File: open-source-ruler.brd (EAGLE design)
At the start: 86 x 54 mm, 65 parts, among them IC1 LT1007CS8, IC2 FT232RLSSOP, IC3 MDC3105DMT1, IC4 XMEGA16A4A, IC5 LFXP20E_XXF256, IC7 ADSP_BF531, Q4 ASF1, U1 V_REG_317DPACK, U2 ATMEGA168, U3 ATMEGA168MLF, U4 7432SE, X1 MINI-USB-UX60A-MB-5ST

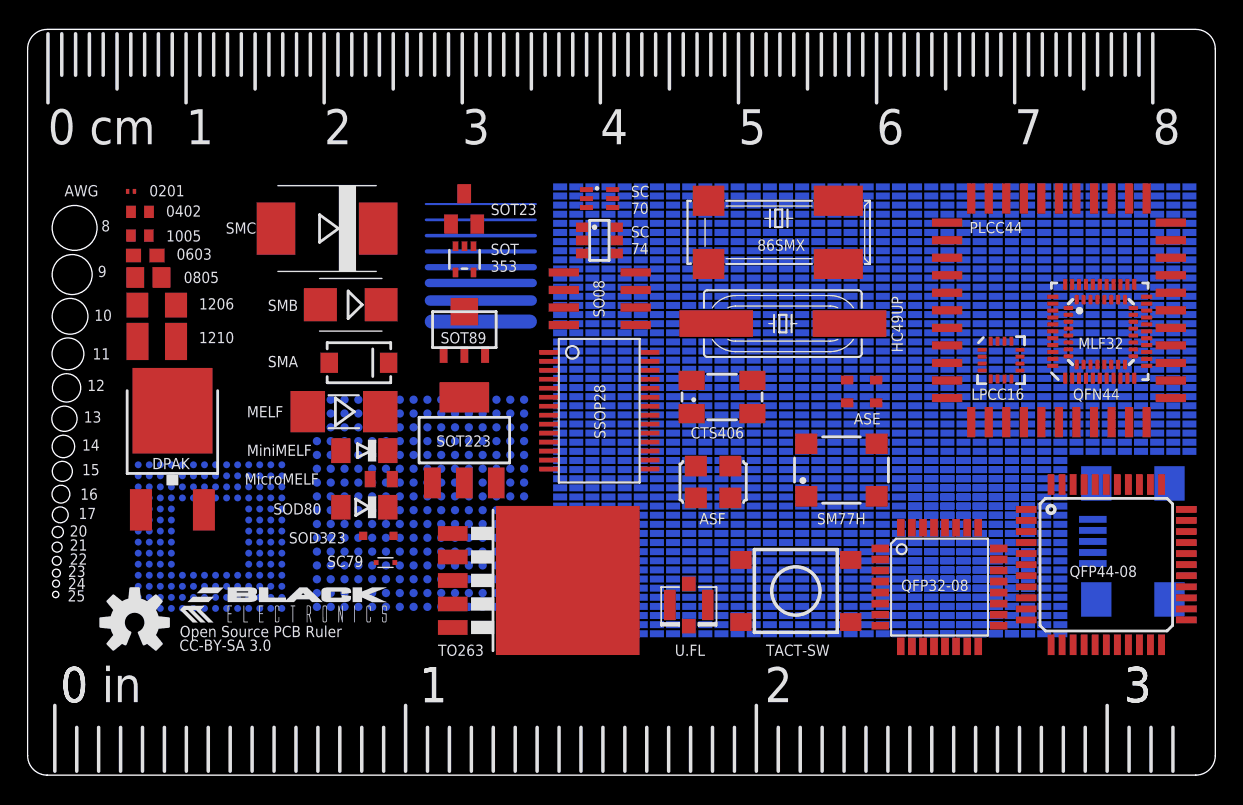
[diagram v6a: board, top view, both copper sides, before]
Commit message: Fixed #5-#11 issues
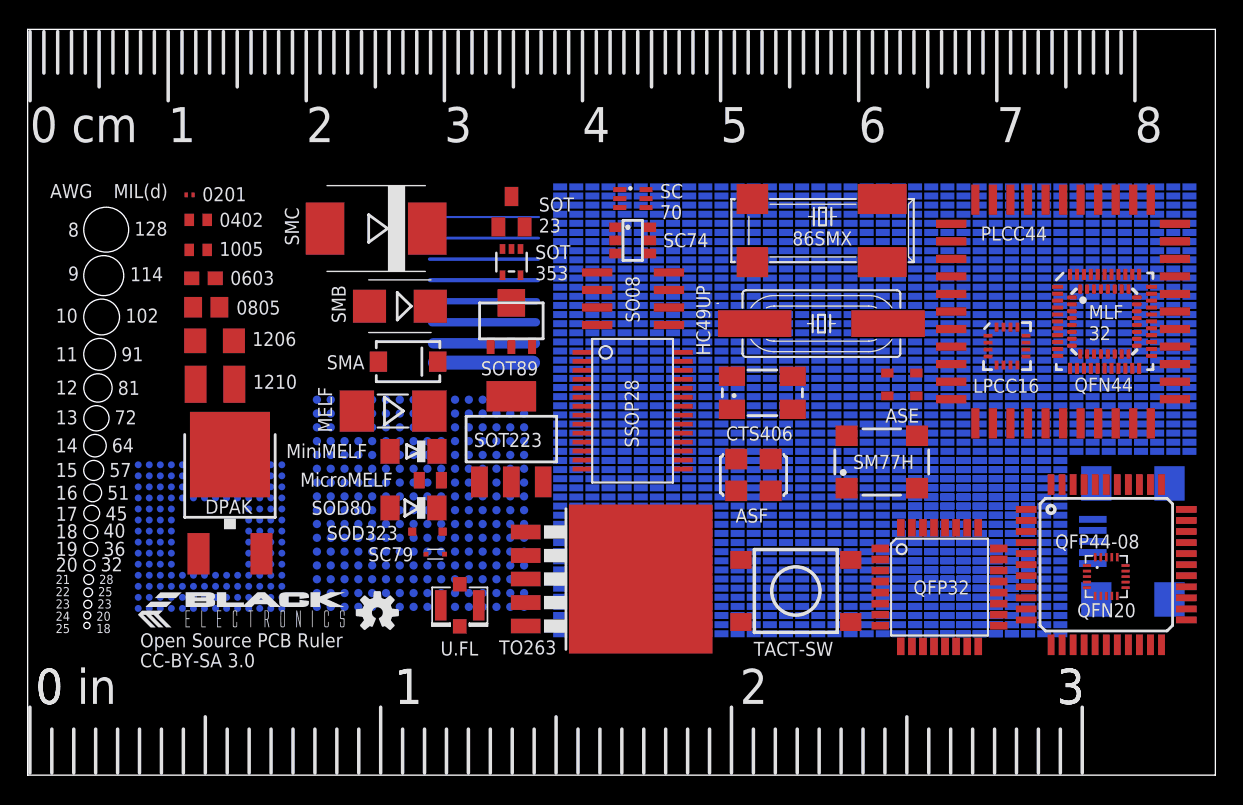
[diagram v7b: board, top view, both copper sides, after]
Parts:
- removed U$28: OSHW-LOGOM, SparkFun:OSHW-LOGO-M
- added QFN20: (no value), SparkFun:QFN-20-0.4MM
- added U$1: OSHW-LOGOS, SparkFun:OSHW-LOGO-S
- moved U$26 16.6 mm to (31.3, 12.3)
- moved IC9 5.28 mm to (41.9, 14.2)
- moved U1 5.24 mm to (14.6, 20.8)
- moved 1210 5.23 mm to (13.6, 28.3)
- moved 1206 4.93 mm to (13.5, 31.5)
- moved 0805 4.71 mm to (12.9, 33.9)
- moved 0603 4.53 mm to (12.7, 36.0)
- moved 1005 4.34 mm to (12.3, 38.0)
- moved 0402 4.26 mm to (12.4, 40.2)
- moved 0201 4.25 mm to (11.7, 42.0)
- moved SC79 3.66 mm to (29.5, 16.0)
- moved D2 3.57 mm to (29.0, 17.6)
- moved D5 3.56 mm to (27.0, 34.0)
- moved D1 3.56 mm to (29.2, 21.4)
- moved D4 3.56 mm to (27.5, 29.9)
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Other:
- outline, holes or cut-outs redrawn
- board text added: "10 10 10 10 10 10 10 10"
- board text added: "102"
- board text added: "114"
- board text added: "128"
- board text added: "19"
- board text added: "28"
- board text added: "32"
- board text added: "36"
- board text added: "45"
- board text added: "51"
- board text added: "57"
- board text added: "6 8 10 12 18 24 30 40"
- board text added: "64"
- board text added: "72"
- board text added: "81"
- board text added: "91"
- board text added: "COLOR CODE BLACK BROWN RED ORANGE YELLOW GREEN BLUE VIOLET GRAY WHITE"
- board text added: "MIL(d)"
- board text added: "MLF 32"
- board text added: "QFN20"
- board text added: "QFP32"
- board text added: "SC74"
- board text added: "SOT 23"
- board text added: "TERA GIGA MEGA KILO milli micro nano pico"
- board text added: "TRACE WIDTH"
- board text removed: "30"
- board text removed: "Colour Code BLACK BROWN RED ORANGE YELLOW GREEN BLUE VIOLET GRAY WHITE"
- board text removed: "GIGA"
- board text removed: "KILO"
- board text removed: "MEGA"
- board text removed: "MLF32"
- board text removed: "QFP32-08"
- board text removed: "SC 74"
- board text removed: "SOT23"
- board text removed: "TERA"
- board text removed: "Trace Width(mil)"
- board text removed: "micro"
- board text removed: "milli"
- board text removed: "nano"
- board text removed: "pico"
